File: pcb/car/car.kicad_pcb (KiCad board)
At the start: 2 copper layers, 60.3 x 63.5 mm, 9 parts

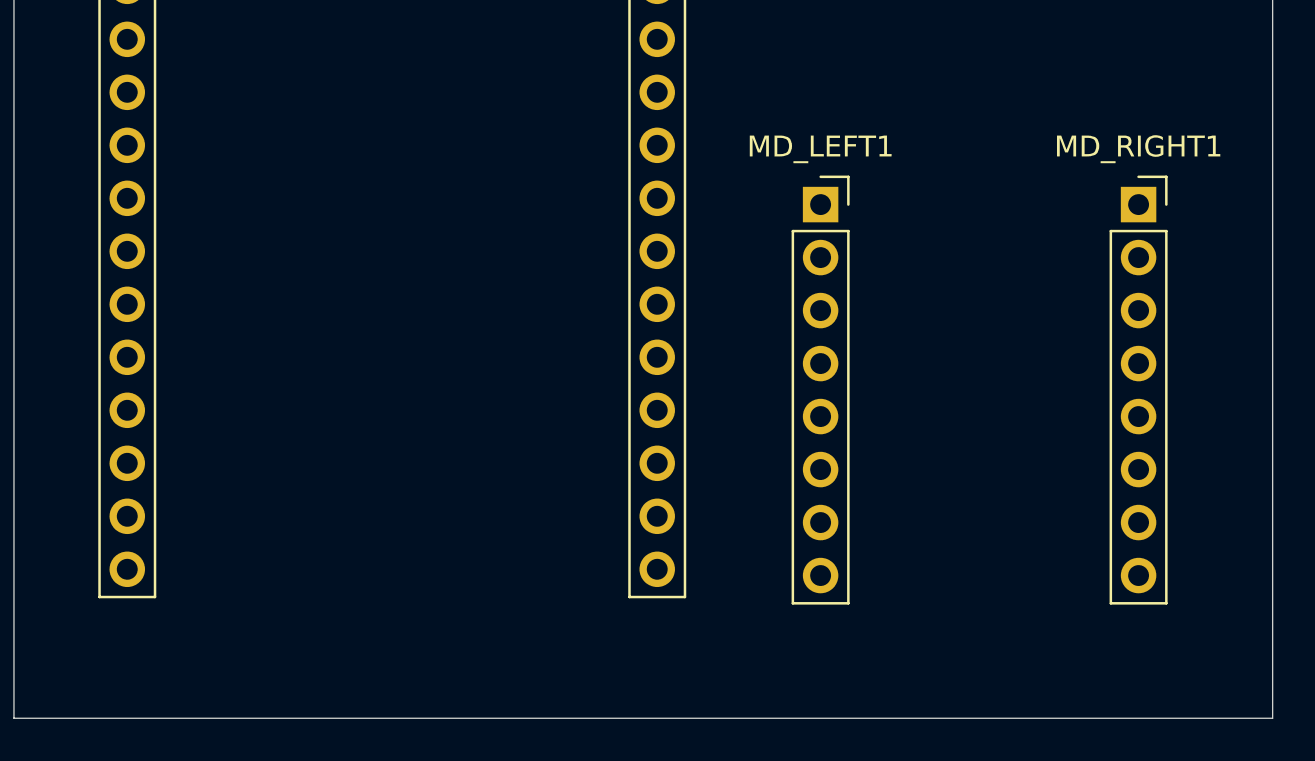
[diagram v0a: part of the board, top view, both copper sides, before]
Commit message: feat: clean up and adding mpu6050
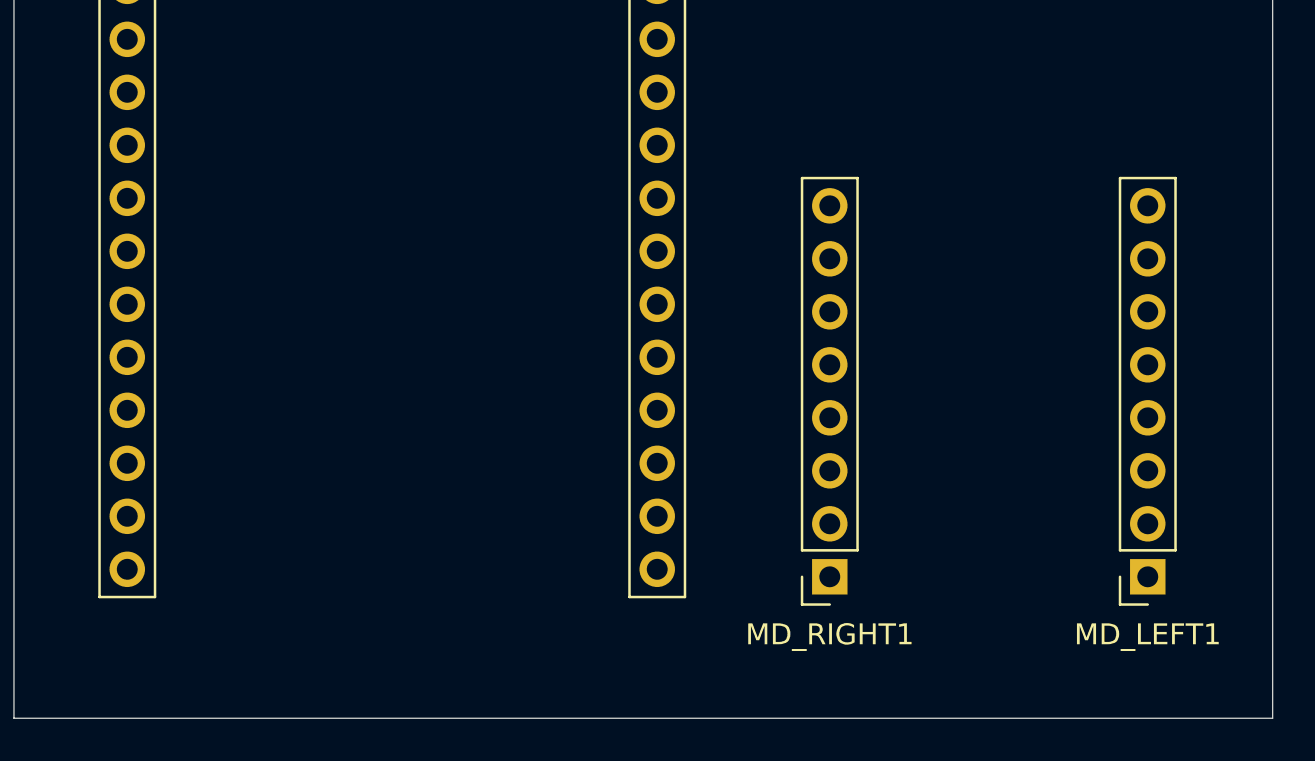
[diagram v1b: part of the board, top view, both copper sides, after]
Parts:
- moved MD_LEFT1 23.8 mm to (123.8, 99.4), turned to 180 degrees
- moved MD_RIGHT1 23.2 mm to (108.6, 99.4), turned to 180 degrees

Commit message: feat: cleaning up pdb
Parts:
- moved ESP32_LEFT1 33.4 mm to (98.1, 96.8), turned to 180 degrees
- moved ESP32_RIGHT1 33.4 mm to (72.7, 96.8), turned to 180 degrees
- moved MD_LEFT1 25.9 mm to (108.0, 78.9), turned to 0 degrees
- moved MD_RIGHT1 25.2 mm to (123.2, 78.9), turned to 0 degrees
- moved BBL1 2.90 mm to (109.7, 61.7)
- moved BBR1 2.90 mm to (118.4, 61.9)
- moved BTL1 2.90 mm to (109.6, 53.9)
- moved BTR1 2.90 mm to (118.4, 53.9)
- moved SERVO1 0.94 mm to (95.6, 45.7)
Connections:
- BBL1 pad 1: -BATT -> GND
- ESP32_LEFT1 pad 1: +3V3 -> +3.3V
- ESP32_LEFT1 pad 10: /AIN2 -> /D19
- ESP32_LEFT1 pad 11: /AIN1 -> /BIN1
- ESP32_LEFT1 pad 14: /D22 -> /BIN2
- ESP32_LEFT1 pad 9: /D18 -> /AIN1
- ESP32_RIGHT1 pad 6: /BIN2 -> /AIN2
- ESP32_RIGHT1 pad 7: /BIN1 -> /D26
- MD_LEFT1 pad 6: /B02 -> GND
- MD_LEFT1 pad 7: /B01 -> /+
- MD_RIGHT1 pad 1: /D18 -> /D14
- MD_RIGHT1 pad 4: /D22 -> /D19
- MD_RIGHT1 pad 7: /D25 -> /D23
- SERVO1 pad 1: /A01 -> GND
- SERVO1 pad 2: /A02 -> +3.3V
- SERVO1 pad 3: /D34 -> /D33
- SERVO1 pad 4: +3V3 -> /+
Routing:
- net GND: track 0.00 -> 218.4 mm
- net +5V: track 0.00 -> 153.6 mm
- net /D14: track 0.00 -> 94.7 mm
- net /AIN2: track 0.00 -> 90.8 mm
- net /AIN1: track 0.00 -> 71.5 mm
- net /BIN2: track 0.00 -> 69.7 mm
- net /D19: track 0.00 -> 68.8 mm
- net /D23: track 0.00 -> 68.5 mm
- net /BIN1: track 0.00 -> 67.6 mm
- net +3.3V: track 0.00 -> 59.1 mm
- net /D33: track 0.00 -> 55.7 mm
- net /+: track 0.00 -> 51.1 mm
- net +BATT: track 0.00 -> 21.4 mm

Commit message: feat: cleaning up pcb
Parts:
- moved BTL1 4.21 mm to (110.6, 49.8)
- moved BTR1 4.15 mm to (119.1, 49.8)
- moved BBL1 3.34 mm to (110.6, 64.9)
- moved BBR1 3.09 mm to (119.1, 64.9)
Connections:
- ESP32_LEFT1 pad 11: /BIN1 -> /AIN1
- ESP32_LEFT1 pad 14: /BIN2 -> /AIN2
- ESP32_LEFT1 pad 9: /AIN1 -> /BIN1
- ESP32_RIGHT1 pad 6: /AIN2 -> /BIN2
- MD_LEFT1 pad 1: +BATT -> /D23
- MD_LEFT1 pad 2: +5V -> /AIN2
- MD_LEFT1 pad 3: GND -> /AIN1
- MD_LEFT1 pad 4: /A01 -> /D19
- MD_LEFT1 pad 5: /A02 -> /BIN1
- MD_LEFT1 pad 6: GND -> /BIN2
- MD_LEFT1 pad 7: /+ -> /D14
- MD_RIGHT1 pad 1: /D14 -> +BATT
- MD_RIGHT1 pad 2: /AIN2 -> +5V
- MD_RIGHT1 pad 3: /AIN1 -> GND
- MD_RIGHT1 pad 4: /D19 -> /+
- MD_RIGHT1 pad 5: /BIN1 -> GND
- MD_RIGHT1 pad 6: /BIN2 -> GND
- MD_RIGHT1 pad 7: /D23 -> /B1
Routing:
- net GND: track 218.4 -> 0.19 mm
- net /AIN2: track 90.8 -> 21.8 mm
- net /AIN1: track 71.5 -> 16.8 mm
- net /D19: track 68.8 -> 16.9 mm
- net /BIN1: track 67.6 -> 16.9 mm
- net /D14: track 94.7 -> 45.4 mm
- net /D23: track 68.5 -> 22.9 mm
- net +5V: track 153.6 -> 116.9 mm
- net /BIN2: track 69.7 -> 46.2 mm
- net +BATT: track 21.4 -> 15.8 mm
- net +3.3V: track 59.1 -> 57.0 mm
- net /+: track 51.1 -> 49.8 mm
- added copper zone on B.Cu, net GND
- added copper zone on F.Cu, net GND

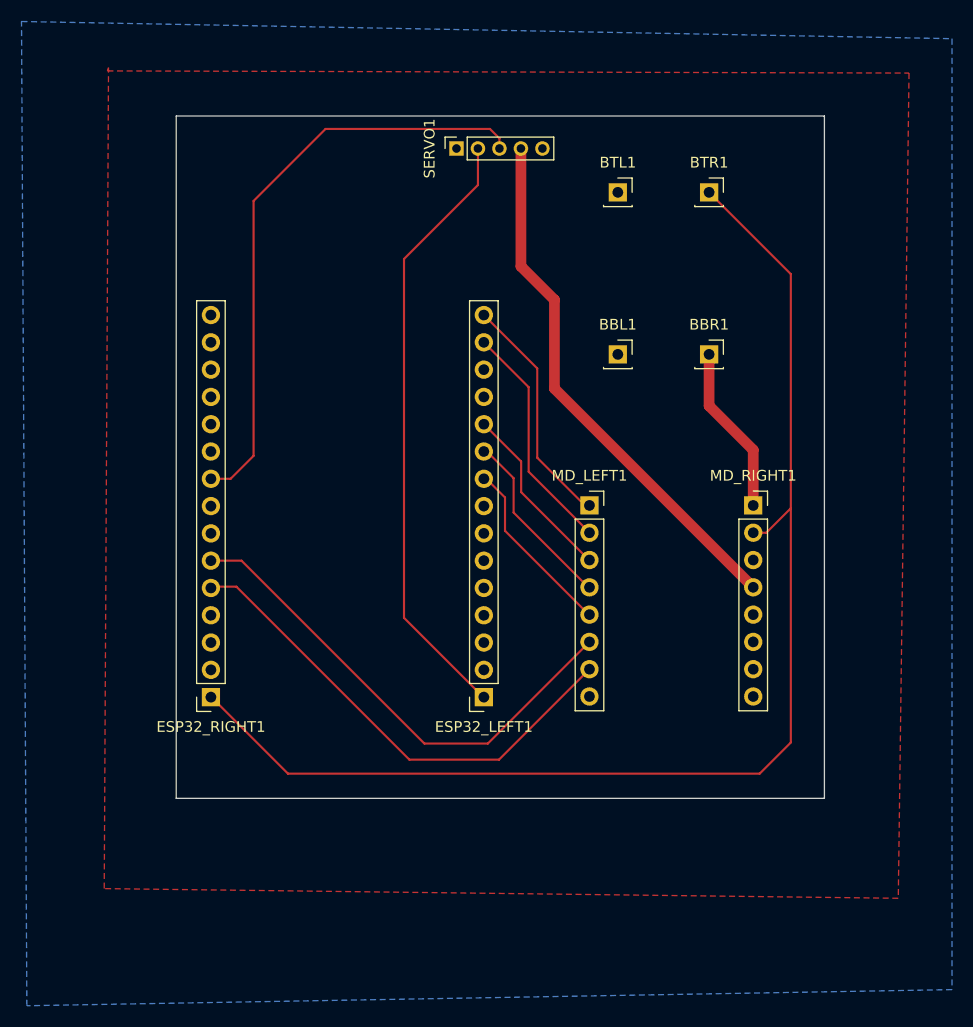
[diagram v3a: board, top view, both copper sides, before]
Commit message: feat: increasing trace width
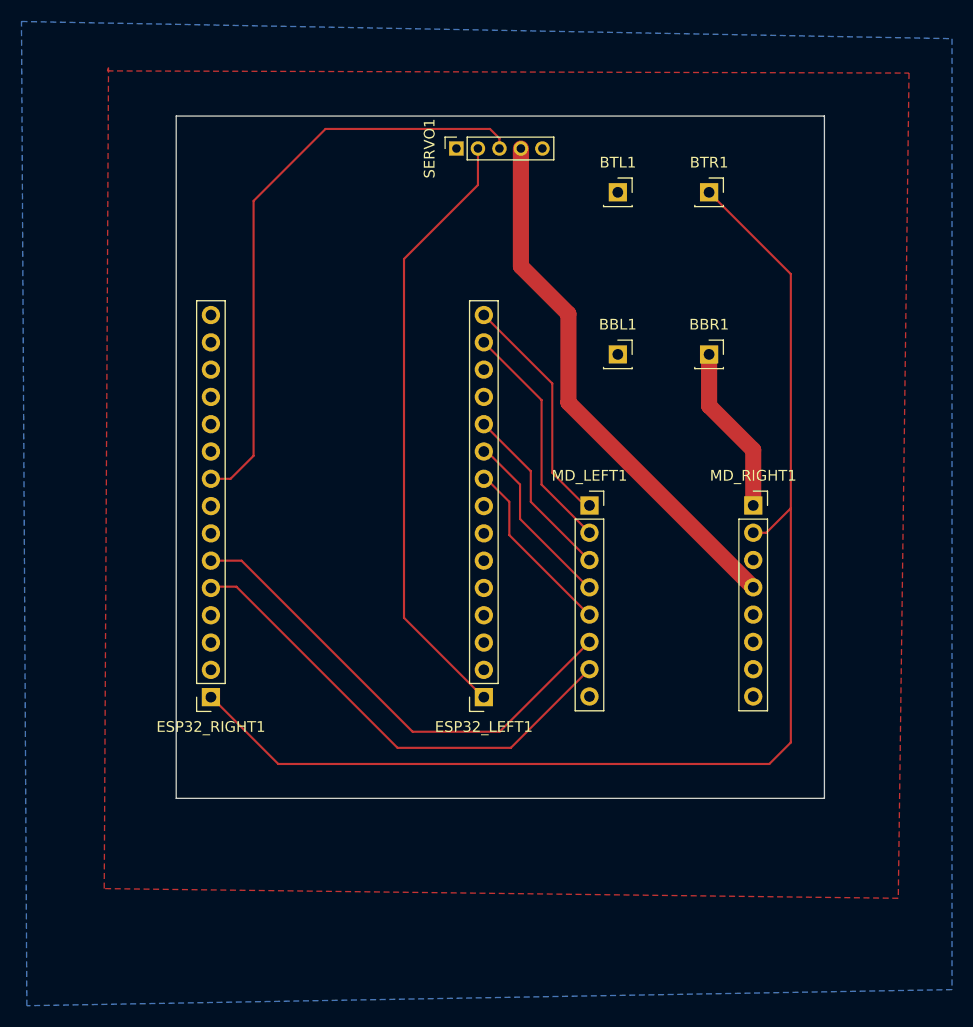
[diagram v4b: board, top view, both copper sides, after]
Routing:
- net /BIN2: track 46.2 -> 45.3 mm
- net /D14: track 45.4 -> 44.5 mm
- net +5V: track 116.9 -> 116.2 mm
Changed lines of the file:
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@@
 			(outputformat 1)
 			(mirror no)
-			(drillshape 1)
+			(drillshape 0)
 			(scaleselection 1)
 			(outputdirectory "")
@@
 	)
 	(segment
-		(start 123.8 103.9)
-		(end 126.7 101)
-		(width 0.2)
-		(layer "F.Cu")
-		(net 3)
-	)
-	(segment
 		(start 126.7 79.2)
 		(end 126.7 57.406875)
@@
 	)
 	(segment
+		(start 124.42 81.48)
+		(end 126.7 79.2)
+		(width 0.2)
+		(layer "F.Cu")
+		(net 3)
+	)
+	(segment
+		(start 79 103)
+		(end 124.7 103)
+		(width 0.2)
+		(layer "F.Cu")
+		(net 3)
+	)
+	(segment
+		(start 126.7 57.406875)
+		(end 119.093125 49.8)
+		(width 0.2)
+		(layer "F.Cu")
+		(net 3)
+	)
+	(segment
+		(start 123.2 81.48)
+		(end 124.42 81.48)
+		(width 0.2)
+		(layer "F.Cu")
+		(net 3)
+	)
+	(segment
+		(start 123.2 81.48)
+		(end 123.22 81.5)
+		(width 0.2)
+		(layer "F.Cu")
+		(net 3)
+	)
+	(segment
+		(start 124.7 103)
+		(end 126.7 101)
+		(width 0.2)
+		(layer "F.Cu")
+		(net 3)
+	)
+	(segment
 		(start 72.73 96.78)
 		(end 72.78 96.78)
@@
 	)
 	(segment
-		(start 124.42 81.48)
-		(end 126.7 79.2)
-		(width 0.2)
-		(layer "F.Cu")
-		(net 3)
-	)
-	(segment
 		(start 126.7 101)
 		(end 126.7 79.2)
@@
 	)
 	(segment
-		(start 126.7 57.406875)
-		(end 119.093125 49.8)
+		(start 72.78 96.78)
+		(end 79 103)
 		(width 0.2)
 		(layer "F.Cu")
@@
 	)
 	(segment
-		(start 123.2 81.48)
-		(end 124.42 81.48)
-		(width 0.2)
-		(layer "F.Cu")
-		(net 3)
-	)
-	(segment
-		(start 123.2 81.48)
-		(end 123.22 81.5)
-		(width 0.2)
-		(layer "F.Cu")
-		(net 3)
-	)
-	(segment
-		(start 72.78 96.78)
-		(end 79.9 103.9)
-		(width 0.2)
-		(layer "F.Cu")
-		(net 3)
-	)
-	(segment
-		(start 79.9 103.9)
-		(end 123.8 103.9)
-		(width 0.2)
-		(layer "F.Cu")
-		(net 3)
-	)
-	(segment
-		(start 100.9 76.4)
+		(start 101.5 77)
 		(end 98.42 73.92)
-		(width 0.2)
-		(layer "F.Cu")
-		(net 4)
-	)
-	(segment
-		(start 100.9 79.6)
-		(end 100.9 76.4)
-		(width 0.2)
-		(layer "F.Cu")
-		(net 4)
-	)
-	(segment
-		(start 107.86 86.56)
-		(end 100.9 79.6)
 		(width 0.2)
 		(layer "F.Cu")
@@
 	)
 	(segment
+		(start 101.5 80.2)
+		(end 101.5 77)
+		(width 0.2)
+		(layer "F.Cu")
+		(net 4)
+	)
+	(segment
+		(start 107.86 86.56)
+		(end 101.5 80.2)
+		(width 0.2)
+		(layer "F.Cu")
+		(net 4)
+	)
+	(segment
 		(start 90.7 56)
 		(end 90.7 89.4)
@@
 	)
 	(segment
-		(start 101.6 74.85)
-		(end 98.13 71.38)
+		(start 107.92 84.02)
+		(end 102.5 78.6)
 		(width 0.2)
 		(layer "F.Cu")
@@
 	)
 	(segment
-		(start 107.92 84.02)
-		(end 101.6 77.7)
+		(start 102.5 78.6)
+		(end 102.5 75.75)
 		(width 0.2)
 		(layer "F.Cu")
@@
 	)
 	(segment
-		(start 101.6 77.7)
-		(end 101.6 74.85)
+		(start 102.5 75.75)
+		(end 98.13 71.38)
 		(width 0.2)
 		(layer "F.Cu")
@@
 	)
 	(segment
-		(start 100.1 78.2)
+		(start 100.5 78.6)
 		(end 98.36 76.46)
 		(width 0.2)
@@
 	)
 	(segment
-		(start 107.9 89.1)
-		(end 100.1 81.3)
-		(width 0.2)
-		(layer "F.Cu")
-		(net 7)
-	)
-	(segment
 		(start 107.96 89.1)
 		(end 107.9 89.1)
@@
 	)
 	(segment
-		(start 100.1 81.3)
-		(end 100.1 78.2)
+		(start 100.5 81.7)
+		(end 100.5 78.6)
 		(width 0.2)
 		(layer "F.Cu")
@@
 	)
 	(segment
+		(start 107.9 89.1)
+		(end 100.5 81.7)
+		(width 0.2)
+		(layer "F.Cu")
+		(net 7)
+	)
+	(segment
 		(start 107.96 81.46)
-		(end 102.3 75.8)
+		(end 103.5 77)
+		(width 0.2)
+		(layer "F.Cu")
+		(net 8)
+	)
+	(segment
+		(start 103.5 69.13)
+		(end 98.13 63.76)
+		(width 0.2)
+		(layer "F.Cu")
+		(net 8)
+	)
+	(segment
+		(start 103.5 77)
+		(end 103.5 69.13)
 		(width 0.2)
 		(layer "F.Cu")
@@
 	)
 	(segment
-		(start 102.3 67.93)
-		(end 98.13 63.76)
-		(width 0.2)
-		(layer "F.Cu")
-		(net 8)
-	)
-	(segment
-		(start 102.3 75.8)
-		(end 102.3 67.93)
-		(width 0.2)
-		(layer "F.Cu")
-		(net 8)
-	)
-	(segment
 		(start 107.96 91.64)
-		(end 98.5 101.1)
+		(end 99.6 100)
 		(width 0.2)
 		(layer "F.Cu")
@@
 	)
 	(segment
-		(start 92.6 101.1)
-		(end 75.58 84.08)
-		(width 0.2)
-		(layer "F.Cu")
-		(net 9)
-	)
-	(segment
-		(start 98.5 101.1)
-		(end 92.6 101.1)
+		(start 99.6 100)
+		(end 91.5 100)
 		(width 0.2)
 		(layer "F.Cu")
@@
 	)
 	(segment
+		(start 91.5 100)
+		(end 75.58 84.08)
+		(width 0.2)
+		(layer "F.Cu")
+		(net 9)
+	)
+	(segment
 		(start 119.093125 69.673125)
 		(end 123.2 73.78)
-		(width 1)
+		(width 1.5)
 		(layer "F.Cu")
 		(net 11)
@@
 		(start 119.093125 64.88125)
 		(end 119.093125 69.673125)
-		(width 1)
+		(width 1.5)
 		(layer "F.Cu")
 		(net 11)
@@
 		(start 123.2 73.78)
 		(end 123.2 78.94)
-		(width 1)
+		(width 1.5)
 		(layer "F.Cu")
 		(net 11)
 	)
 	(segment
-		(start 91.2 102.6)
-		(end 75.1 86.5)
-		(width 0.2)
-		(layer "F.Cu")
-		(net 16)
-	)
-	(segment
-		(start 99.54 102.6)
-		(end 91.2 102.6)
+		(start 107.96 94.18)
+		(end 100.64 101.5)
 		(width 0.2)
 		(layer "F.Cu")
@@
 	)
 	(segment
+		(start 100.64 101.5)
+		(end 90.1 101.5)
+		(width 0.2)
+		(layer "F.Cu")
+		(net 16)
+	)
+	(segment
 		(start 75.1 86.5)
 		(end 72.85 86.5)
@@
 	)
 	(segment
-		(start 107.96 94.18)
-		(end 99.54 102.6)
+		(start 90.1 101.5)
+		(end 75.1 86.5)
 		(width 0.2)
 		(layer "F.Cu")
@@
 	)
 	(segment
-		(start 107.54 78.94)
-		(end 103.1 74.5)
+		(start 104.5 75.9)
+		(end 104.5 67.59)
+		(width 0.2)
+		(layer "F.Cu")
+		(net 26)
+	)
+	(segment
+		(start 104.5 67.59)
+		(end 98.13 61.22)
 		(width 0.2)
 		(layer "F.Cu")
@@
 	)
 	(segment
+		(start 107.54 78.94)
+		(end 104.5 75.9)
+		(width 0.2)
+		(layer "F.Cu")
+		(net 26)
+	)
+	(segment
+		(start 98.8 61)
+		(end 98.35 61)
+		(width 0.2)
+		(layer "F.Cu")
+		(net 26)
+	)
+	(segment
+		(start 107.96 78.94)
+		(end 107.92 78.9)
+		(width 0.2)
+		(layer "F.Cu")
+		(net 26)
+	)
+	(segment
 		(start 107.96 78.94)
 		(end 107.54 78.94)
@@
 	)
 	(segment
-		(start 98.8 61)
-		(end 98.35 61)
-		(width 0.2)
-		(layer "F.Cu")
-		(net 26)
-	)
-	(segment
-		(start 107.96 78.94)
-		(end 107.92 78.9)
-		(width 0.2)
-		(layer "F.Cu")
-		(net 26)
-	)
-	(segment
-		(start 103.1 74.5)
-		(end 103.1 66.19)
-		(width 0.2)
-		(layer "F.Cu")
-		(net 26)
-	)
-	(segment
-		(start 103.1 66.19)
-		(end 98.13 61.22)
-		(width 0.2)
-		(layer "F.Cu")
-		(net 26)
-	)
-	(segment
 		(start 98.13 68.84)
 		(end 98.1 68.87)
@@
 	)
 	(segment
-		(start 104.7 68.06)
+		(start 123.2 86.566999)
 		(end 123.2 86.56)
-		(width 1)
-		(layer "F.Cu")
-		(net 30)
-	)
-	(segment
-		(start 104.7 59.807215)
-		(end 104.7 68.06)
-		(width 1)
+		(width 1.5)
 		(layer "F.Cu")
 		(net 30)
@@
 		(start 101.58 45.72)
 		(end 101.58 56.687215)
-		(width 1)
+		(width 1.5)
 		(layer "F.Cu")
 		(net 30)
@@
 	(segment
 		(start 101.58 56.687215)
-		(end 104.7 59.807215)
-		(width 1)
+		(end 106 61.107215)
+		(width 1.5)
 		(layer "F.Cu")
 		(net 30)
+	)
+	(segment
+		(start 106 69.366999)
+		(end 123.2 86.566999)
+		(width 1.5)
+		(layer "F.Cu")
+		(net 30)
+	)
+	(segment
+		(start 106 61.107215)
+		(end 106 69.366999)
+		(width 1.5)
+		(layer "F.Cu")
+		(net 30)
